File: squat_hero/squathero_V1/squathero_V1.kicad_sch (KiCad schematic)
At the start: 6 parts, among them U2 AMS1117

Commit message: V1 squat hero
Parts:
- removed D1: H5VUT1B, PCM_JLCPCB:SOT-143-4_L2.9-W1.3-P1.90-LS2.4-BL-1, symbol PCM_JLCPCB-Diode-Packages:Package, H5VUT1B
- removed FB1: ~, PCM_JLCPCB:FB_0805, symbol PCM_JLCPCB-Inductors:Ferrite,0805
- removed U1: ~, JLCPCB_USB-C:USB-SMD_TYPE-C16PIN-1, symbol JLCPCB_USB-C:12402012E212A
- removed U2: AMS1117, PCM_JLCPCB:SOT-223-3_L6.5-W3.4-P2.30-LS7.0-BR, symbol PCM_JLCPCB-Power:LDO, 3.3V, 1A
- added C1, C3, C4, C5: 1uF, Resistor_SMD:R_0805_2012Metric, symbol Device:C
- added C2: 10nF, Resistor_SMD:R_0805_2012Metric, symbol Device:C
- added D1: White, PCM_JLCPCB:D_0805, symbol PCM_JLCPCB-Diodes:LED,0805,White
- added D2: Yellow, PCM_JLCPCB:D_0805, symbol PCM_JLCPCB-Diodes:LED,0805,Yellow
- added D3: Green, PCM_JLCPCB:D_0805, symbol PCM_JLCPCB-Diodes:LED,0805,Green
- added D4: Red, PCM_JLCPCB:D_0603, symbol PCM_JLCPCB-Diodes:LED,0603,Red
- added D5, D6: 1N5819WS, PCM_JLCPCB:D_SOD-323, symbol PCM_JLCPCB-Diodes:Schottky,1N5819WS
- added D7, D8: H3V3L10B, PCM_JLCPCB:D_DFN1006-2L, symbol PCM_JLCPCB-Diodes:TVS-Bi,H3V3L10B
- added FB2: ~, PCM_JLCPCB:FB_0805, symbol PCM_JLCPCB-Inductors:Ferrite,0805
- added J1: Conn_01x03, Connector_PinSocket_2.54mm:PinSocket_1x03_P2.54mm_Vertical, symbol Connector_Generic:Conn_01x03
- added J3, J4, J5: Conn_01x02, Connector_PinSocket_2.54mm:PinSocket_1x02_P2.54mm_Vertical, symbol Connector_Generic:Conn_01x02
- added Q1, Q2, Q3: HL2307, PCM_JLCPCB:Q_SOT-23, symbol PCM_JLCPCB-Transistors:PMOS,HL2307
- added R10: 2.5k, Resistor_SMD:R_0805_2012Metric, symbol Device:R
- added R11, R3, R6: 10k, Resistor_SMD:R_0805_2012Metric, symbol Device:R
- added R12, R13: 330, Resistor_SMD:R_0805_2012Metric, symbol Device:R
- added R4, R5: 4.7k, Resistor_SMD:R_0805_2012Metric, symbol Device:R
- added R7, R8: 50, Resistor_SMD:R_0805_2012Metric, symbol Device:R
- added R9: 1k, Resistor_SMD:R_0805_2012Metric, symbol Device:R
- added S1: Tactile Button, 160gf, PCM_JLCPCB:SW-SMD_4P-L5.1-W5.1-P3.70-LS6.5-TL-2, symbol PCM_JLCPCB-Connectors_Buttons:Tactile Button, 160gf
- added U1: ~, JLCPCB_USB_FOOTPRINT:USB-SMD_TYPE-C16PIN-1, symbol JLCPCB_USBC:12402012E212A
- added U2: ~, esp_32:WIFIM-SMD_ESP32-C3-MINI-1, symbol esp_32:ESP32-C3-MINI-1-N4
- added U3: AMS1117-3.3, Package_TO_SOT_SMD:SOT-223-3_TabPin2, symbol Regulator_Linear:AMS1117-3.3
- added U4: ~, imu:LGA-14_L3.0-W2.5-P0.50-TL_QMI8658A, symbol imu:BMI323
- added U5: TP4057, PCM_JLCPCB:SOT-23-6_L2.9-W1.6-P0.95-LS2.8-BL, symbol PCM_JLCPCB-Power:Battery, Li-Ion, 0.5A, TP4057
- added U6: ~, batt_conn:Untitled, symbol batt_conn:3.7V_batt_pads
- R1, R2: footprint Resistor_SMD:R_0805_2012Metric -> Resistor_SMD:R_0201_0603Metric
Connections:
- net +5V: now also C5.1, D5.2, FB2.1, FB2.2, Q3.1 (G), R11.1, R9.1, U1.A4B9 (VBUS), U1.B4A9 (VBUS), U5.4 (VCC)
- net CC1: now also U1.A5 (CC1)
- net CC2: now also U1.B5 (CC2)
- net GND: now also C1.2, C2.2, C3.2, C4.2, C5.2, J1.1 (Pin_1), J3.1 (Pin_1), J4.1 (Pin_1), R10.2, R11.2, R7.2, R8.2, S1.3 (C), S1.4 (D), U1.17, U1.18, U1.19, U1.20, U1.A1B12 (GND), U1.B1A12 (GND), U2.1 (GND), U2.11 (GND), U2.14 (GND), U2.2 (GND), U2.36 (GND), U2.37 (GND), U2.38 (GND), U2.39 (GND), U2.40 (GND), U2.41 (GND), U2.42 (GND), U2.43 (GND), U2.44 (GND), U2.45 (GND), U2.46 (GND), U2.47 (GND), U2.48 (GND), U2.49 (GND), U2.50 (GND), U2.51 (GND), U2.52 (GND), U2.53 (GND), U3.1 (GND), U4.1 (SDO), U4.6 (GNDIO), U4.7 (GND), U5.2 (GND), U6.2 (3.7V-)
- net USB_D+: now also D7.1, D7.2, U1.A6 (D+), U1.B6 (D+), U2.27 (IO19)
- net USB_D-: now also D8.1, D8.2, U1.A7 (D-), U1.B7 (D-), U2.26 (IO18)
- new net: J3.2 (Pin_2), Q1.3 (D)
- new net: J1.3 (Pin_3), R12.1
- new net: D1.1, R7.1
- new net: J4.2 (Pin_2), Q2.3 (D)
- new net: J1.2 (Pin_2), R13.1
- new net: D2.1, R8.1
- new net +3.3V: C1.1, C2.1, Q1.2 (S), Q2.2 (S), R3.1, R4.2, R5.2, R6.1, U2.3 (3V3), U3.2 (VO), U4.5 (VDDIO), U4.8 (VDD)
- new net BATT+: C4.1, D6.2, Q3.2 (S), Q3.3 (D), U5.3 (BAT), U6.1 (3.7V+)
- new net BATT_: D3.2, D4.2, R9.2
- new net BATT_CHRG: D4.1, U5.1 (CHRG)
- new net BATT_PROG: R10.1, U5.6 (PROG)
- new net BATT_STDBY: D3.1, U5.5 (STDBY)
- new net DEBUG_LED1: D1.2, U2.6 (IO3)
- new net DEBUG_LED2: D2.2, U2.5 (IO2)
- new net EN: R6.2, S1.1 (A), S1.2 (B), U2.8 (EN)
- new net GPI0_1: R13.2, U2.13 (IO1)
- new net GPI0_10: R12.2, U2.16 (IO10)
- new net I2C_INT1: U2.20 (IO6), U4.4 (INT1)
- new net I2C_INT2: U2.19 (IO5), U4.9 (INT2)
- new net I2C_SCL_1: R4.1, U2.12 (IO0), U4.14 (SDX)
- new net I2C_SDA_1: R5.1, U2.18 (IO4), U4.13 (SCX)
- new net PWM_1: Q1.1 (G), U2.23 (IO9)
- new net PWM_2: Q2.1 (G), U2.21 (IO7)
- new net PWR_FLT: C3.1, R3.2
- new net raw_power: D5.1, D6.1, J5.1 (Pin_1), J5.2 (Pin_2), U3.3 (VI)
- no-connect marks 2 -> 3
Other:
- note added: "Haptic Motor Pins"
- note added: "IMU / I2C Interface"
- note added: "Open GPIO"
- moved on the sheet: R1, R2

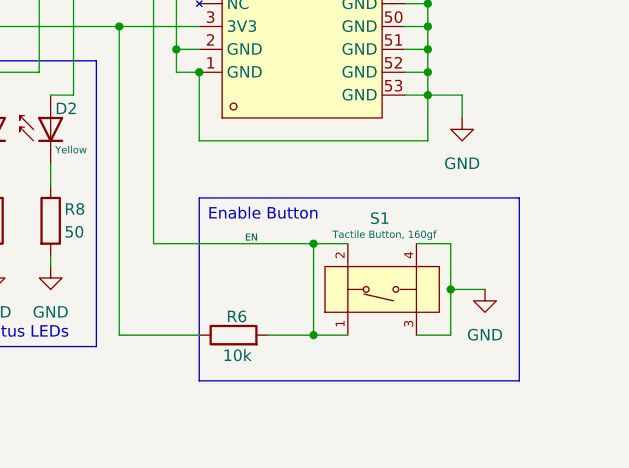
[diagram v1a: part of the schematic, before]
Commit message: all formatted besides power / BMS
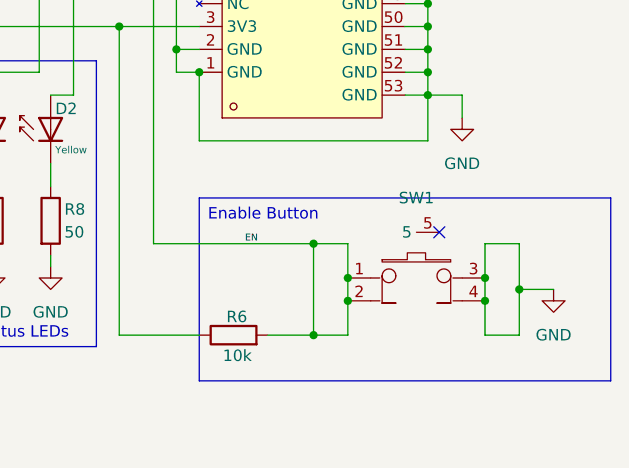
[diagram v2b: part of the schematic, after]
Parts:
- removed S1: Tactile Button, 160gf, PCM_JLCPCB:SW-SMD_4P-L5.1-W5.1-P3.70-LS6.5-TL-2, symbol PCM_JLCPCB-Connectors_Buttons:Tactile Button, 160gf
- added SW1: ~, Button_Switch_SMD:SW-SMD_4P-L3.5-W3.5_PTS840GKPSMTRLFS, symbol JLCPCB_side_button:PTS840GKPSMTRLFS
- R1, R2: footprint Resistor_SMD:R_0201_0603Metric -> Resistor_SMD:R_0603_1608Metric
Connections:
- net EN: now also SW1.1, SW1.2
- net GND: now also SW1.3, SW1.4
- no-connect marks 3 -> 4
